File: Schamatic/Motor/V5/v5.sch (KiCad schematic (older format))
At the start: 47 parts, among them J1 SWD, J10 GND, J11 V, J12 U, J13 W, J2 SPI, J3 RS485, J4 RS485, J5 CAP+, J6 12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

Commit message: new board version ready to order
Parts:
- R9: value 120 -> 200
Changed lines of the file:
@@
 P 1200 3800
 F 0 "R9" V 1280 3800 50  0000 C CNN
-F 1 "120" V 1200 3800 50  0000 C CNN
+F 1 "200" V 1200 3800 50  0000 C CNN
 F 2 "Resistors_SMD:R_0603" V 1130 3800 50  0001 C CNN
 F 3 "" H 1200 3800 50  0001 C CNN

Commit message: new version of the board
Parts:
- D1: footprint Diodes_SMD:D_0805 -> Diodes_SMD:D_0603
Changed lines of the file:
@@
 F 0 "D1" H 1900 3600 50  0000 C CNN
 F 1 "CD0603-B0340R" H 1900 3400 50  0000 C CNN
-F 2 "Diodes_SMD:D_0805" H 1900 3500 50  0001 C CNN
+F 2 "Diodes_SMD:D_0603" H 1900 3500 50  0001 C CNN
 F 3 "" H 1900 3500 50  0001 C CNN
 	1    1900 3500
@@
 L +12V #PWR06
 U 1 1 597768BB
-P 950 1300
-F 0 "#PWR06" H 950 1150 50  0001 C CNN
-F 1 "+12V" H 950 1440 50  0000 C CNN
-F 2 "" H 950 1300 50  0001 C CNN
-F 3 "" H 950 1300 50  0001 C CNN
-	1    950  1300
+P 750 1300
+F 0 "#PWR06" H 750 1150 50  0001 C CNN
+F 1 "+12V" H 750 1440 50  0000 C CNN
+F 2 "" H 750 1300 50  0001 C CNN
+F 3 "" H 750 1300 50  0001 C CNN
+	1    750  1300
 	0    -1   -1   0
 $EndComp
@@
 U 1 1 59C795D7
 P 2650 4500
-F 0 "SW2" H 2600 4800 60  0000 C CNN
+F 0 "SW2" V 2600 4800 60  0000 C CNN
 F 1 "SWiTCH" H 2650 4950 60  0000 C CNN
 F 2 "Resistors_SMD:R_1206" H 2650 4500 60  0001 C CNN
@@
 	1    0    0    -1
 $EndComp
+Wire Wire Line
+	950  1300 750  1300
 $EndSCHEMATC

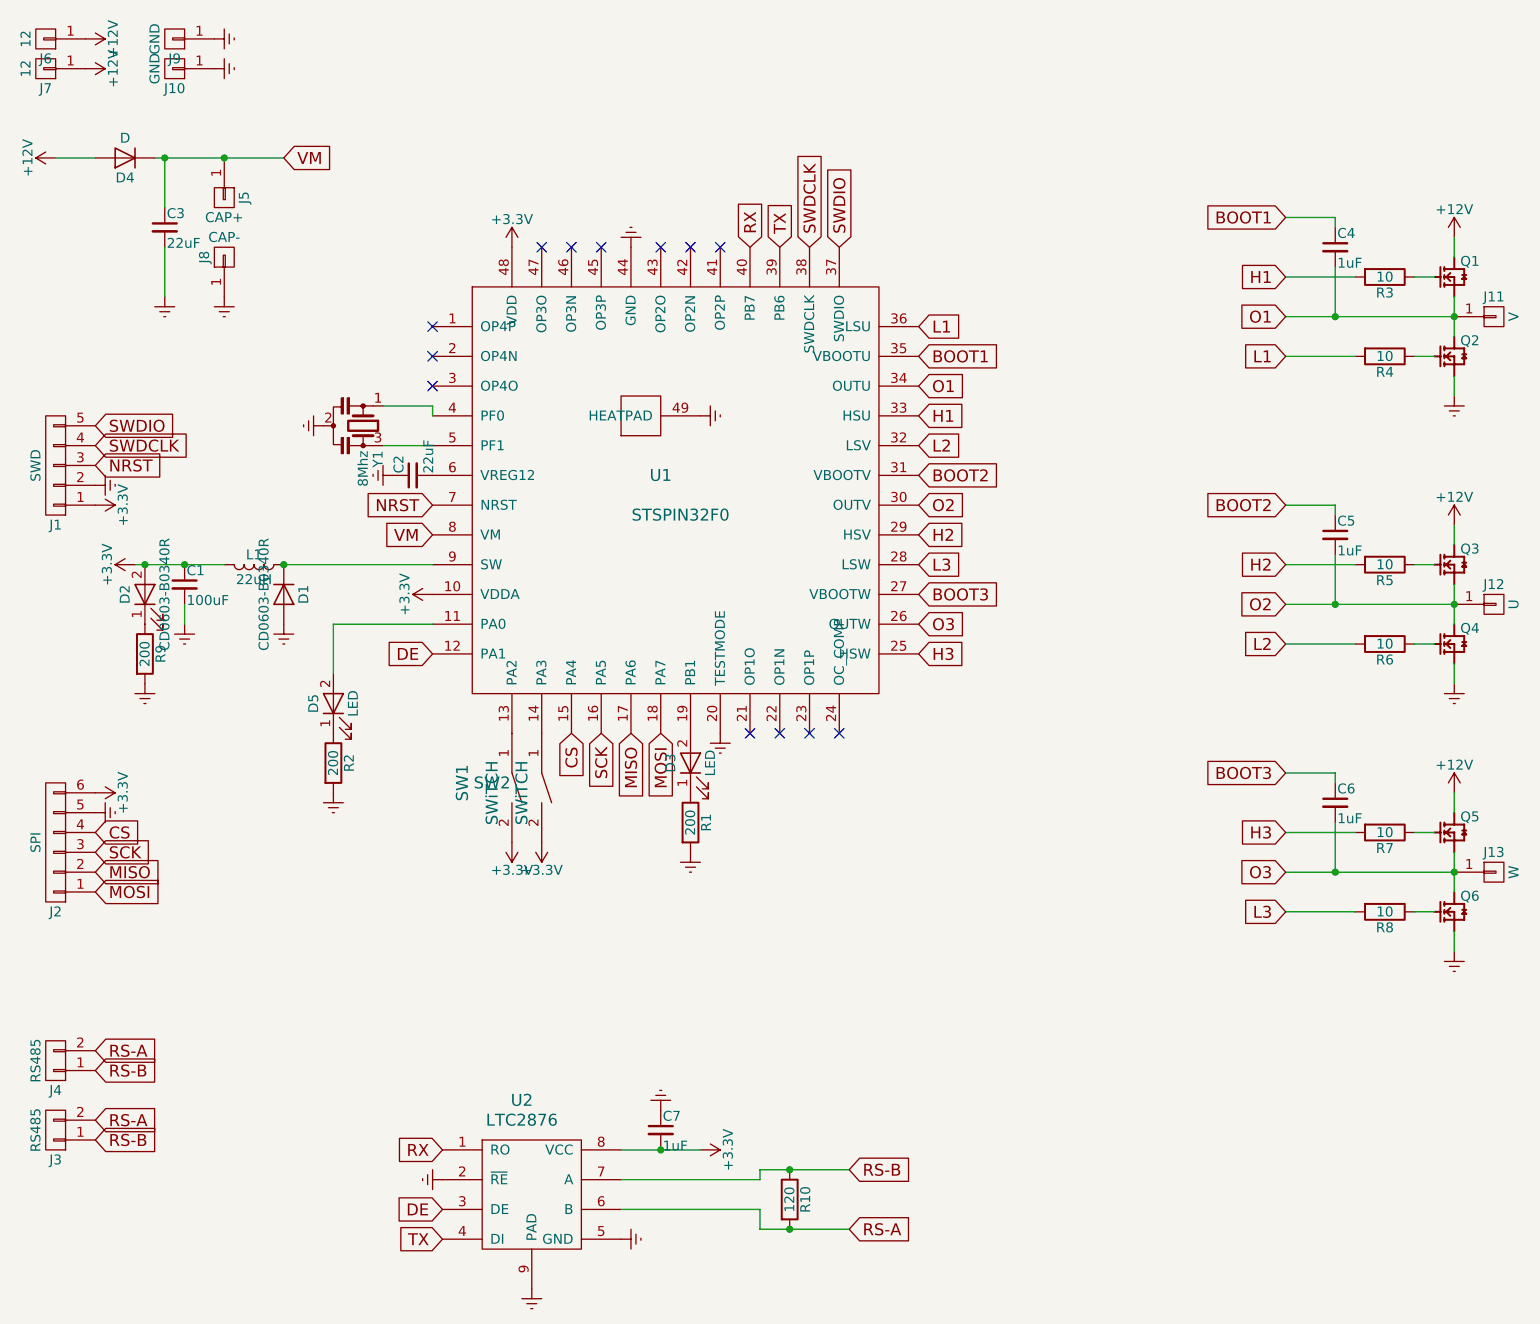
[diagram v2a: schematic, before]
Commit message: motor PCB optimization
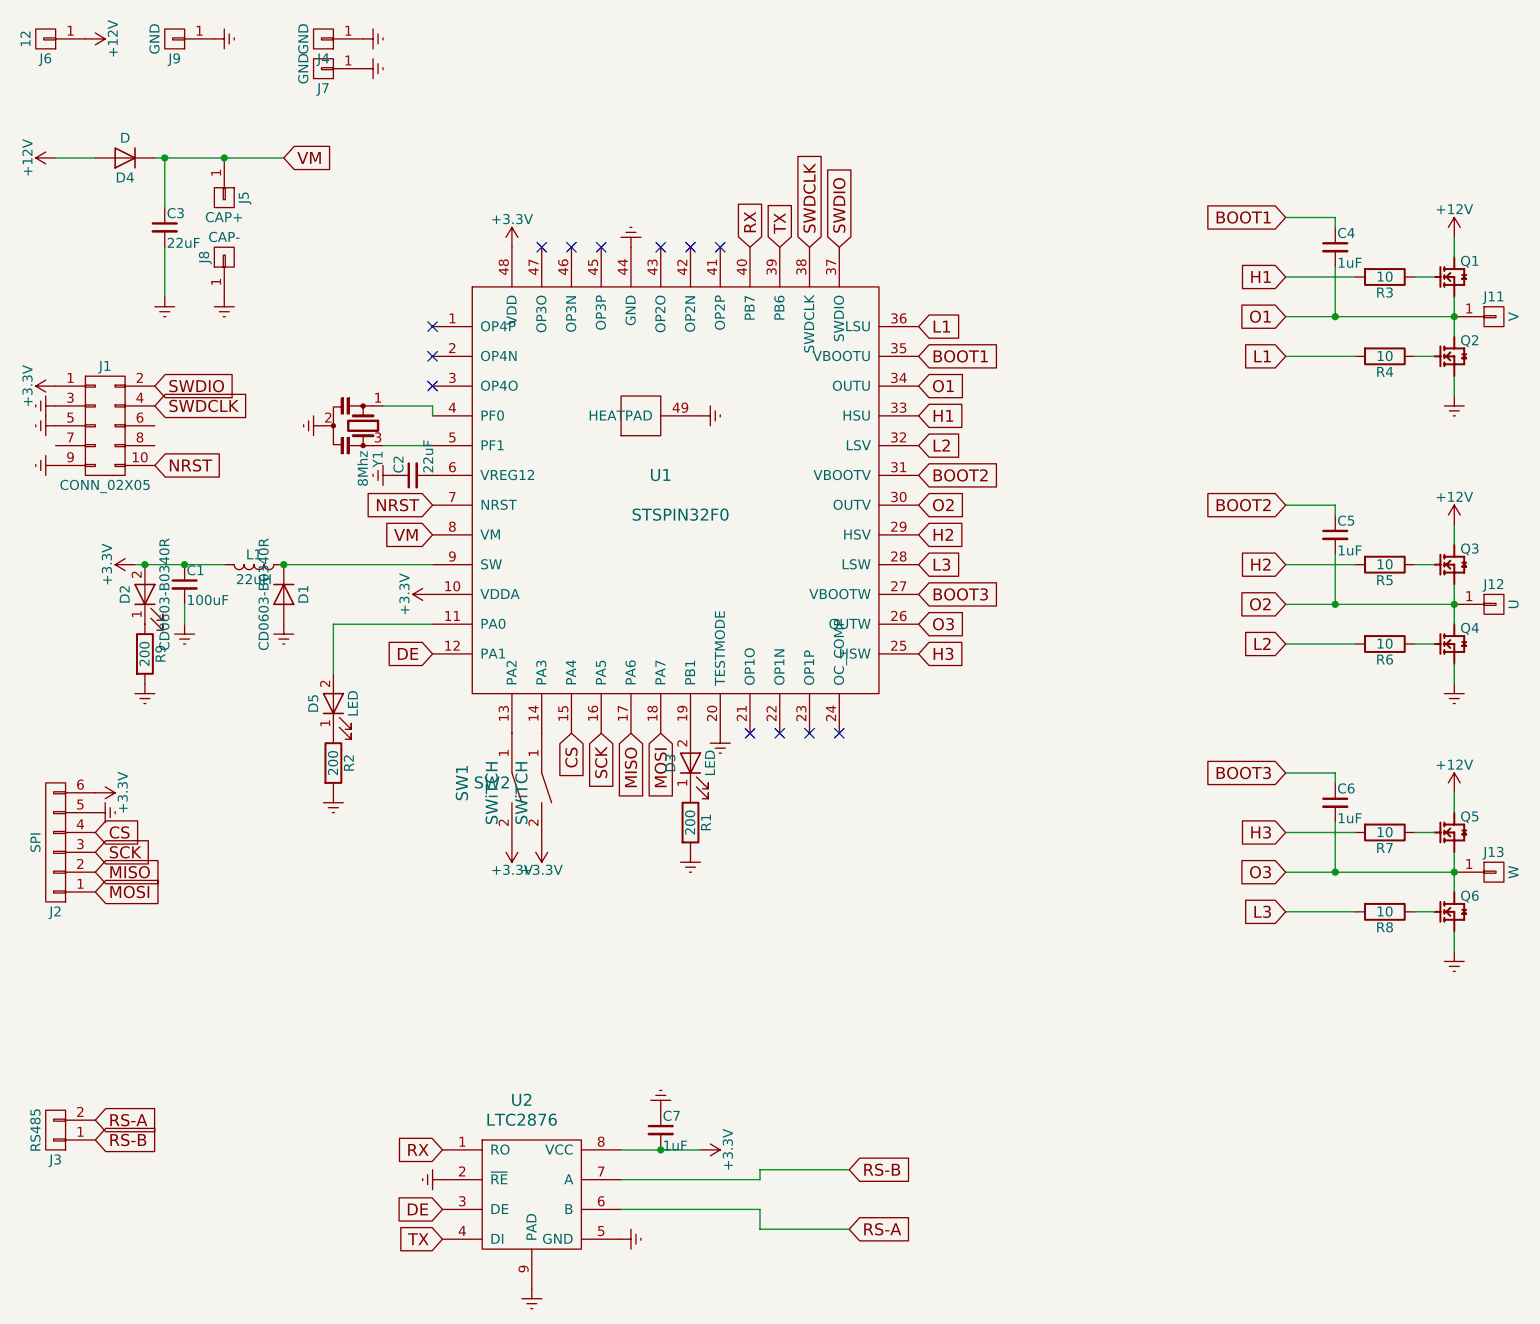
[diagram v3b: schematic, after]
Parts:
- removed J1: SWD, Pin_Headers:Pin_Header_Straight_1x05_Pitch2.54mm, symbol CONN_01X05
- removed J10: GND, Pin_Headers:Pin_Header_Straight_1x01_Pitch2.54mm, symbol CONN_01X01
- removed J4: RS485, Pin_Headers:Pin_Header_Straight_1x02_Pitch2.54mm, symbol CONN_01X02
- removed R10: 120, Resistors_SMD:R_0603, symbol R
- added J1: CONN_02X05, Pin_Headers:Pin_Header_Straight_2x05_Pitch1.27mm, symbol CONN_02X05
- added J4: GND, Pin_Headers:Pin_Header_Straight_1x01_Pitch2.54mm, symbol CONN_01X01
- J7: value 12 -> GND
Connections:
- net +12V: no longer J7.1 (P1)
- net +3V3: now also J1.1 (P1)
- net Earth: now also J7.1 (P1), J1.3 (P3), J1.5 (P5), J1.9 (P9), J4.1 (P1)
- net NRST: now also J1.10 (P10)
- net SWDCLK: now also J1.4 (P4)
- net SWDIO: now also J1.2 (P2)
